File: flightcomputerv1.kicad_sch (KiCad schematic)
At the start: 51 parts, among them IC1 MMC5983MA, J1 Screw_Terminal_01x02, J2 Screw_Terminal_01x02, J3 Conn_01x12, J4 Conn_01x12, J5 Conn_01x02, J6 Conn_01x24, J7 Conn_01x24, M1 Motor_Servo, M2 Motor_Servo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

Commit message: small update
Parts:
- added SW2: SLW-913535-2A-SMT, HPRfootprints:SLW-913535_CUD, symbol HPRsymbols:SLW-913535-2A-SMT
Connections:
- net GND: now also SW2.2, SW2.3, SW2.5, SW2.6
- net SENSE_miso: now also J3.1 (Pin_1)
- net SENSE_mosi: now also J3.2 (Pin_2)
- net SENSE_sck: now also J3.3 (Pin_3)
- net baro_cs: now also J3.10 (Pin_10)
- net imu_accel_cs: now also J3.6 (Pin_6)
- net imu_accel_int1: now also J3.7 (Pin_7)
- net imu_gyro_cs: now also J3.8 (Pin_8)
- net imu_gyro_int1: now also J3.9 (Pin_9)
- net mag_cs: now also J3.4 (Pin_4)
- net mag_int: now also J3.5 (Pin_5)
- net teensy_onoff: now reaches U1.54 (ON_OFF)
- net teensy_onoff: now also SW2.1, SW2.4
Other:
- note added: "Teensy ON/OFF Switch"
- note added: "surface mount antenna connector"
- note removed: "continuity check? high side driver isntead?"
- note removed: "surface mount antenna connector?"
- moved on the sheet: BZ1, D1, D2, D3, M1, M2, R10, R11, R9

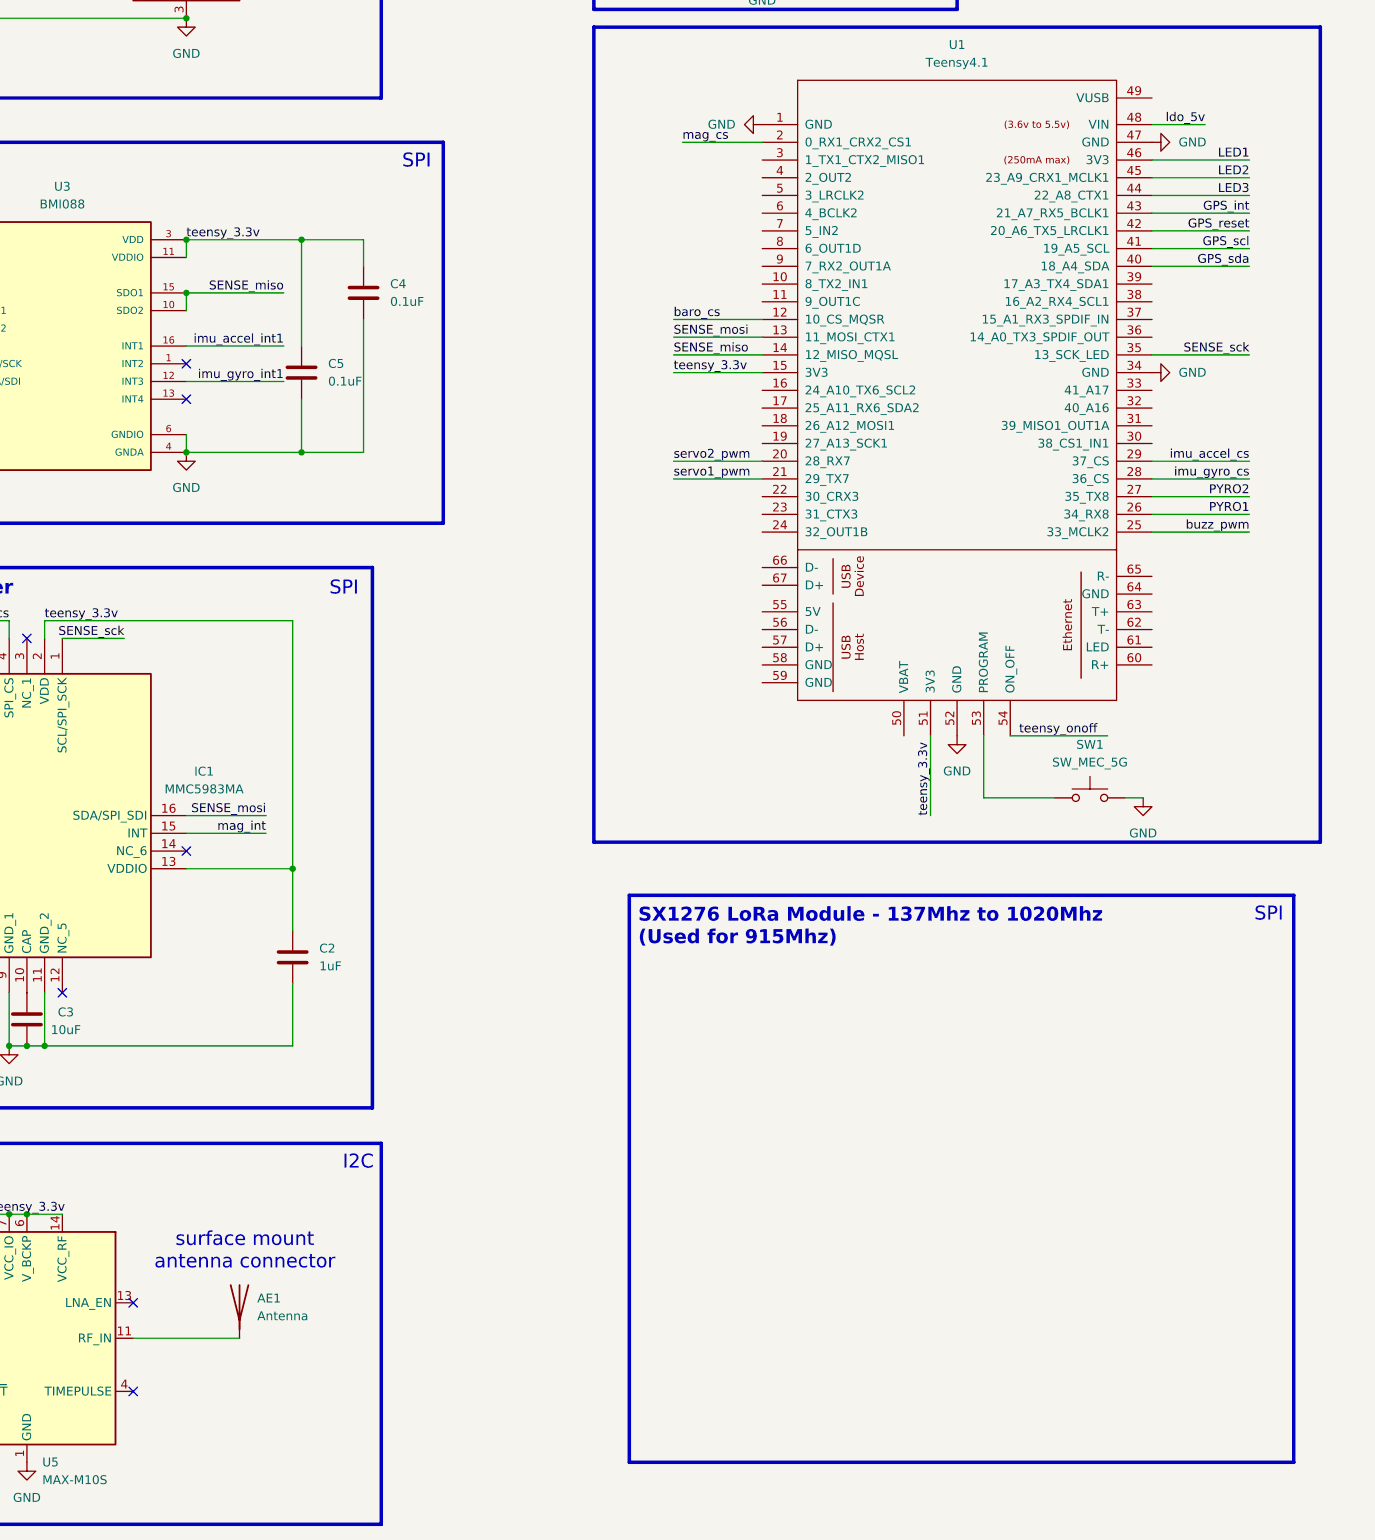
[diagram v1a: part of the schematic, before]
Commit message: added radio module, still need footprint for either xbee or adafruit rfm95 breakout
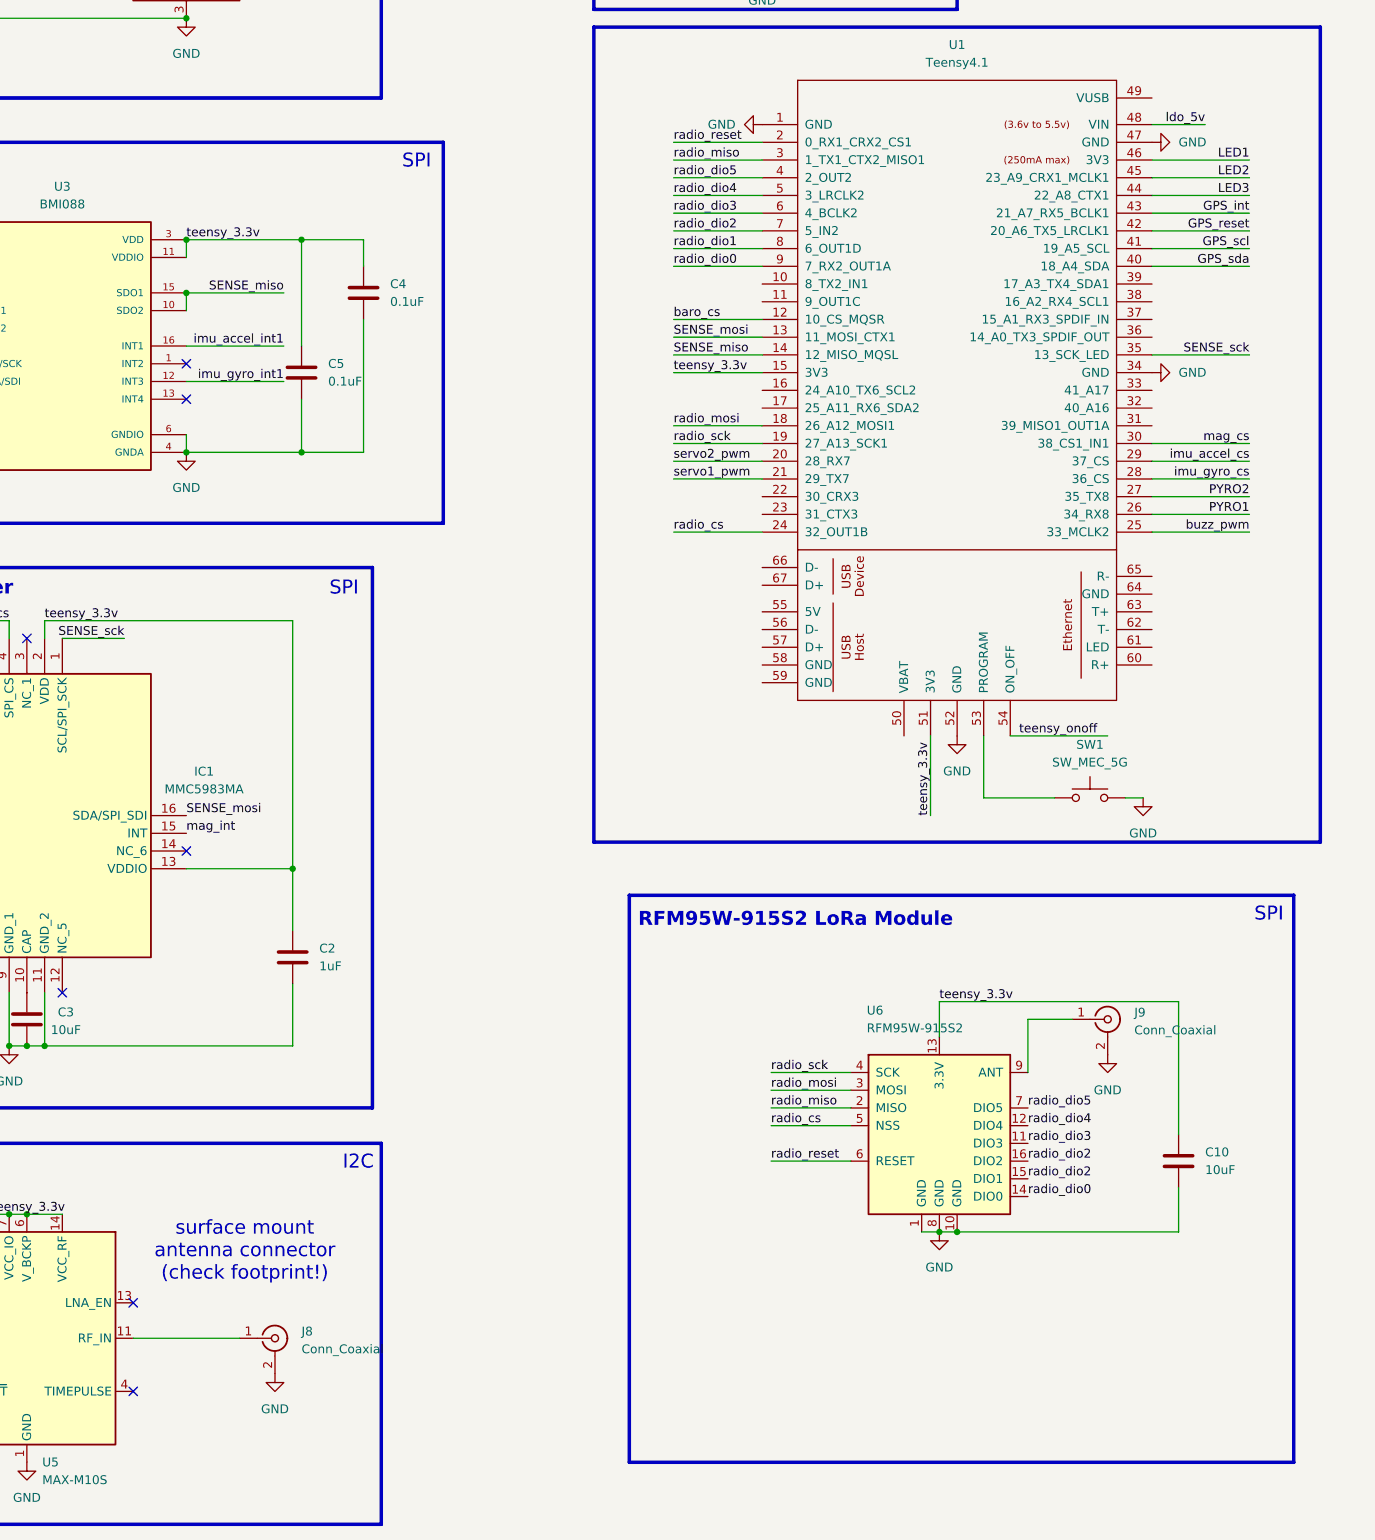
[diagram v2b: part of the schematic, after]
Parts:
- removed AE1: Antenna, symbol Device:Antenna
- added C10: 10uF, symbol Device:C
- added J8, J9: Conn_Coaxial, Connector_Coaxial:SMA_Amphenol_132134-10_Vertical, symbol Connector:Conn_Coaxial
- added U6: RFM95W-915S2, RF_Module:HOPERF_RFM9XW_SMD, symbol RF_Module:RFM95W-915S2
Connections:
- net GND: now also C10.2, J8.2 (Ext), J9.2 (Ext), U6.1 (GND), U6.10 (GND), U6.8 (GND)
- net mag_cs: now also U1.30 (38_CS1_IN1); no longer U1.2 (0_RX1_CRX2_CS1)
- net teensy_3.3v: now also C10.1, U6.13 (3.3V)
- net radio_mosi: now reaches U1.18 (26_A12_MOSI1)
- net radio_mosi: now also U6.3 (MOSI)
- net radio_sck: now reaches U1.19 (27_A13_SCK1)
- net radio_sck: now also U6.4 (SCK)
- net radio_cs: now reaches U1.24 (32_OUT1B)
- net radio_cs: now also U6.5 (NSS)
- net radio_miso: now reaches U1.3 (1_TX1_CTX2_MISO1)
- net radio_miso: now also U6.2 (MISO)
- net radio_dio5: now reaches U1.4 (2_OUT2)
- net radio_dio5: now also U6.7 (DIO5)
- net radio_dio4: now reaches U1.5 (3_LRCLK2)
- net radio_dio4: now also U6.12 (DIO4)
- net radio_dio3: now reaches U1.6 (4_BCLK2)
- net radio_dio3: now also U6.11 (DIO3)
- net radio_dio2: now reaches U1.7 (5_IN2)
- net radio_dio2: now also U6.15 (DIO1), U6.16 (DIO2)
- net radio_dio1: now reaches U1.8 (6_OUT1D)
- net radio_dio0: now reaches U1.9 (7_RX2_OUT1A)
- net radio_dio0: now also U6.14 (DIO0)
- net at U5.11 (RF_IN): now also J8.1 (In)
- new net: J9.1 (In), U6.9 (ANT)
- new net radio_reset: U1.2 (0_RX1_CRX2_CS1), U6.6 (RESET)
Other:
- note added: "RFM95W-915S2 LoRa Module"
- note added: "surface mount antenna connector (check footprint!)"
- note removed: "SX1276 LoRa Module - 137Mhz to 1020Mhz (Used for 915Mhz)"
- note removed: "surface mount antenna connector"

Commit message: started placement
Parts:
- removed J3, J4: Conn_01x12, Connector_PinHeader_2.54mm:PinHeader_1x12_P2.54mm_Vertical, symbol Connector_Generic:Conn_01x12
- removed R5, R6: 150K, Resistor_SMD:R_0201_0603Metric_Pad0.64x0.40mm_HandSolder, symbol Device:R
- C10: footprint (none) -> Capacitor_SMD:C_0201_0603Metric_Pad0.64x0.40mm_HandSolder
- J5: footprint Connector_JST:JST_XA_B20B-XASK-1-A_1x20_P2.50mm_Vertical -> Connector_JST:JST_XA_B02B-XASK-1-A_1x02_P2.50mm_Vertical
- R10, R11, R9: value R -> 150
- R7, R8: value 100K -> 4.7k
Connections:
- net pyro1_sense is gone; now on net GPS_scl: R8.2
- net pyro2_sense is gone; now on net GPS_sda: R7.2
- net GND: now also J6.1 (Pin_1), J7.10 (Pin_10), J7.23 (Pin_23); no longer R7.1, R8.1
- net GPS_int: now also J7.19 (Pin_19)
- net GPS_reset: now also J7.18 (Pin_18)
- net GPS_scl: now also J7.17 (Pin_17)
- net GPS_sda: now also J7.16 (Pin_16)
- net LED1: now also J7.9 (Pin_9), U1.33 (41_A17); no longer U1.46 (3V3)
- net LED2: now also J7.8 (Pin_8), U1.32 (40_A16); no longer U1.45 (23_A9_CRX1_MCLK1)
- net LED3: now also J7.7 (Pin_7), U1.31 (39_MISO1_OUT1A); no longer U1.44 (22_A8_CTX1)
- net PYRO1: now also J7.2 (Pin_2)
- net PYRO2: now also J7.3 (Pin_3)
- net SENSE_miso: now also J6.14 (Pin_14)
- net SENSE_mosi: now also J6.13 (Pin_13)
- net SENSE_sck: now also J7.11 (Pin_11)
- net baro_cs: now also J6.12 (Pin_12)
- net buzz_pwm: now also J7.1 (Pin_1)
- net imu_accel_cs: now also J7.5 (Pin_5)
- net imu_gyro_cs: now also J7.4 (Pin_4)
- net ldo_5v: now also J7.24 (Pin_24)
- net mag_cs: now also J7.6 (Pin_6)
- net radio_cs: now also J6.24 (Pin_24)
- net radio_dio0: now also J6.9 (Pin_9)
- net radio_dio1: now also J6.8 (Pin_8)
- net radio_dio2: now also J6.7 (Pin_7)
- net radio_dio3: now also J6.6 (Pin_6)
- net radio_dio4: now also J6.5 (Pin_5)
- net radio_dio5: now also J6.4 (Pin_4)
- net radio_miso: now also J6.3 (Pin_3)
- net radio_mosi: now also J6.18 (Pin_18)
- net radio_reset: now also J6.2 (Pin_2)
- net radio_sck: now also J6.19 (Pin_19)
- net servo1_pwm: now also J6.21 (Pin_21)
- net servo2_pwm: now also J6.20 (Pin_20)
- net teensy_3.3v: now also J6.15 (Pin_15), J7.22 (Pin_22), R7.1, R8.1, U1.46 (3V3)
- net FREE1: now reaches U1.10 (8_TX2_IN1)
- net FREE1: now also J6.10 (Pin_10)
- net FREE2: now reaches U1.11 (9_OUT1C)
- net FREE2: now also J6.11 (Pin_11)
- net FREE3: now reaches U1.16 (24_A10_TX6_SCL2)
- net FREE3: now also J6.16 (Pin_16)
- net FREE4: now reaches U1.17 (25_A11_RX6_SDA2)
- net FREE4: now also J6.17 (Pin_17)
- net FREE5: now reaches U1.22 (30_CRX3)
- net FREE5: now also J6.22 (Pin_22)
- net FREE6: now reaches U1.23 (31_CTX3)
- net FREE6: now also J6.23 (Pin_23)
- net FREE12: now reaches U1.36 (14_A0_TX3_SPDIF_OUT)
- net FREE12: now also J7.12 (Pin_12)
- net FREE11: now reaches U1.37 (15_A1_RX3_SPDIF_IN)
- net FREE11: now also J7.13 (Pin_13)
- net FREE10: now reaches U1.38 (16_A2_RX4_SCL1)
- net FREE10: now also J7.14 (Pin_14)
- net FREE9: now reaches U1.39 (17_A3_TX4_SDA1)
- net FREE9: now also J7.15 (Pin_15)
- net FREE8: now reaches J7.20 (Pin_20)
- net FREE8: now also U1.44 (22_A8_CTX1)
- net FREE7: now reaches J7.21 (Pin_21)
- net FREE7: now also U1.45 (23_A9_CRX1_MCLK1)
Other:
- note added: "pyro sense?"
- note removed: "makes sure pyro sense <3.3v"

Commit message: updated placement and routing 2/16
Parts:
- removed SW1: SW_MEC_5G, Button_Switch_SMD:SW_MEC_5GSH9, symbol Switch:SW_MEC_5G
- removed SW2: SLW-913535-2A-SMT, HPRfootprints:SLW-913535_CUD, symbol HPRsymbols:SLW-913535-2A-SMT
- added S1: TS04-66-70-BK-160-SMT, HPRfootprints:SW_TS04-66-70-BK-160-SMT, symbol HPRsymbols:TS04-66-70-BK-160-SMT
- added SW2: SW_Wuerth_450301014042, Button_Switch_THT:SW_Slide-03_Wuerth-WS-SLTV_10x2.5x6.4_P2.54mm, symbol Switch:SW_Wuerth_450301014042
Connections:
- net FREE2 is gone; now on net mag_int: J6.11 (Pin_11), U1.11 (9_OUT1C)
- net FREE3 is gone; now on net imu_accel_int1: J6.16 (Pin_16), U1.16 (24_A10_TX6_SCL2)
- net FREE4 is gone; now on net imu_gyro_int1: J6.17 (Pin_17), U1.17 (25_A11_RX6_SDA2)
- net GND: now also S1.2, S1.4, SW2.2 (C)
- net radio_dio1: now also U6.15 (DIO1)
- net radio_dio2: no longer U6.15 (DIO1)
- net teensy_3.3v: now also S1.3, SW2.3 (A)
- net teensy_onoff: now also SW2.1 (B)
- net at U1.53 (PROGRAM): now also S1.1
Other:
- moved on the sheet: C10, J9, U6
